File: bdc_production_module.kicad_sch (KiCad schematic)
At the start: 20 parts, among them U2 TPS54531DDA

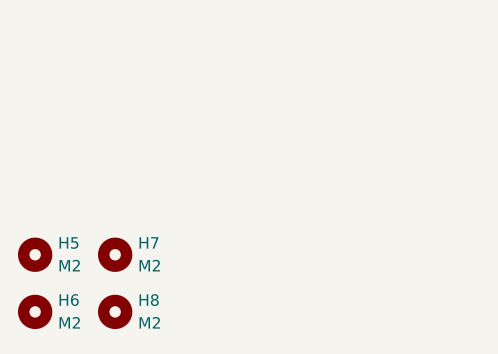
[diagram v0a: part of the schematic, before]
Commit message: copy prototype board layout to production
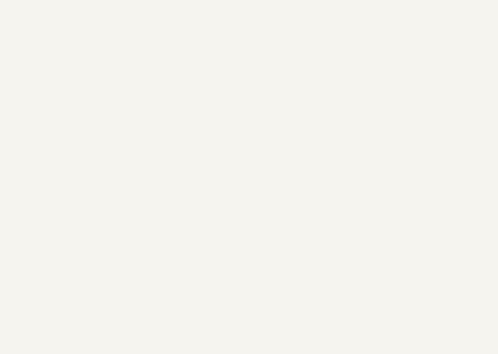
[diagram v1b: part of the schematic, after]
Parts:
- removed H5, H6, H7, H8: M2, MountingHole:MountingHole_2.2mm_M2, symbol Mechanical:MountingHole

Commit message: initial production module layout
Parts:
- added J4: Conn_01x36, Connector_PCBEdge:BUS_PCIexpress_x1, symbol Connector_Generic:Conn_01x36
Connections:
- net GND1: now also J4.A12 (Pin_12), J4.A13 (Pin_13), J4.A14 (Pin_14), J4.A15, J4.A16 (Pin_16), J4.A17 (Pin_17), J4.A18 (Pin_18), J4.B12 (Pin_30), J4.B13 (Pin_31), J4.B14 (Pin_32), J4.B15 (Pin_33), J4.B16 (Pin_34), J4.B17 (Pin_35), J4.B18 (Pin_36)
- net VIN: now also J4.B1 (Pin_19), J4.B10 (Pin_28), J4.B11 (Pin_29), J4.B2 (Pin_20), J4.B3 (Pin_21), J4.B4 (Pin_22), J4.B5 (Pin_23), J4.B6 (Pin_24), J4.B7 (Pin_25), J4.B8 (Pin_26), J4.B9 (Pin_27)
- net VOUT: now also J4.A1 (Pin_1), J4.A10 (Pin_10), J4.A11 (Pin_11), J4.A2 (Pin_2), J4.A3 (Pin_3), J4.A4 (Pin_4), J4.A5 (Pin_5), J4.A6 (Pin_6), J4.A7 (Pin_7), J4.A8 (Pin_8), J4.A9 (Pin_9)
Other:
- moved on the sheet: C11, C12, C13, C14, C15, C16, C17, C18, C19, C20, D2, L2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
